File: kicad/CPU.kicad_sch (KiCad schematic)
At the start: 21 parts, among them J1 Conn_ARM_SWD_TagConnect_TC203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, SW1 SW_Push, U5 STM32F303CBTx, X1 8 MHz

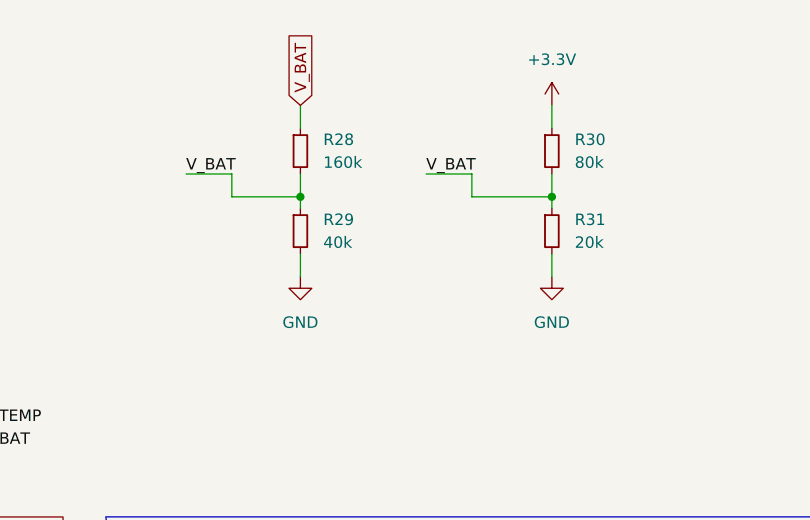
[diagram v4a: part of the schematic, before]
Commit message: [kicad] added thermistor
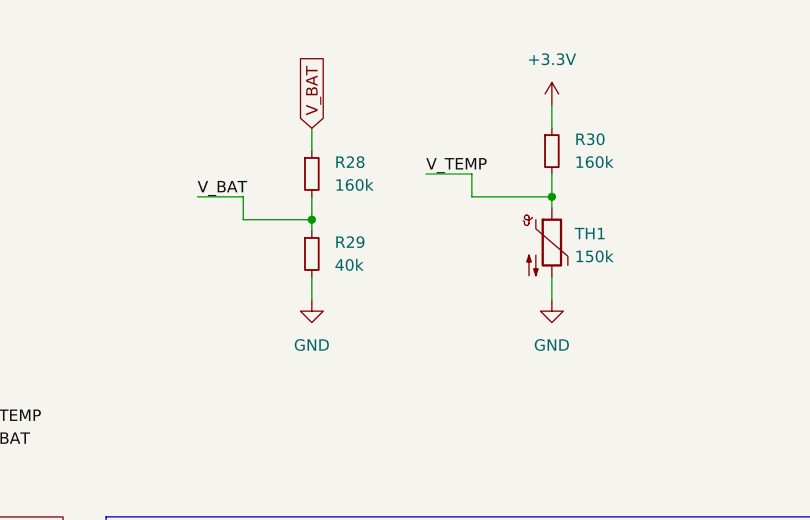
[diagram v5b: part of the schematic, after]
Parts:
- removed R31: 20k, symbol Device:R_Small
- added TH1: 150k, Resistor_SMD:R_0402_1005Metric, symbol Device:Thermistor_NTC
- R30: value 80k -> 160k
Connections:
- net GND: now also TH1.2
- net V_BAT: no longer R30.2
- net V_TEMP: now also R30.2, TH1.1
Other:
- moved on the sheet: R28, R29
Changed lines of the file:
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@@
   (junction (at 85.09 63.5) (diameter 0) (color 0 0 0 0)
   )
-  (junction (at 199.39 34.29) (diameter 0) (color 0 0 0 0)
+  (junction (at 200.66 36.83) (diameter 0) (color 0 0 0 0)
   )
   (junction (at 207.01 82.55) (diameter 0) (color 0 0 0 0)
@@
     (stroke (width 0) (type default))
   )
-  (wire (pts (xy 186.69 31.75) (xy 191.77 31.75))
+  (wire (pts (xy 187.96 34.29) (xy 193.04 34.29))
     (stroke (width 0) (type default))
   )
@@
     (stroke (width 0) (type default))
   )
-  (wire (pts (xy 199.39 34.29) (xy 199.39 35.56))
+  (wire (pts (xy 200.66 36.83) (xy 200.66 38.1))
     (stroke (width 0) (type default))
   )
@@
     (stroke (width 0) (type default))
   )
-  (wire (pts (xy 227.33 40.64) (xy 227.33 43.18))
+  (wire (pts (xy 227.33 43.18) (xy 227.33 45.72))
     (stroke (width 0) (type default))
   )
@@
     (stroke (width 0) (type default))
   )
-  (wire (pts (xy 191.77 34.29) (xy 191.77 31.75))
+  (wire (pts (xy 193.04 36.83) (xy 193.04 34.29))
     (stroke (width 0) (type default))
   )
@@
     (stroke (width 0) (type default))
   )
-  (wire (pts (xy 199.39 40.64) (xy 199.39 43.18))
+  (wire (pts (xy 200.66 43.18) (xy 200.66 45.72))
     (stroke (width 0) (type default))
   )
@@
     (stroke (width 0) (type default))
   )
-  (wire (pts (xy 199.39 34.29) (xy 191.77 34.29))
+  (wire (pts (xy 200.66 36.83) (xy 193.04 36.83))
     (stroke (width 0) (type default))
   )
@@
     (stroke (width 0) (type default))
   )
-  (wire (pts (xy 199.39 24.13) (xy 199.39 26.67))
+  (wire (pts (xy 200.66 26.67) (xy 200.66 29.21))
     (stroke (width 0) (type default))
   )
@@
     (stroke (width 0) (type default))
   )
-  (wire (pts (xy 199.39 31.75) (xy 199.39 34.29))
+  (wire (pts (xy 200.66 34.29) (xy 200.66 36.83))
     (stroke (width 0) (type default))
   )
@@
     (effects (font (size 1.27 1.27)) (justify left bottom))
   )
-  (label "V_BAT" (at 213.36 31.75 0) (fields_autoplaced)
+  (label "V_TEMP" (at 213.36 31.75 0) (fields_autoplaced)
     (effects (font (size 1.27 1.27)) (justify left bottom))
   )
-  (label "V_BAT" (at 186.69 31.75 0) (fields_autoplaced)
+  (label "V_BAT" (at 187.96 34.29 0) (fields_autoplaced)
     (effects (font (size 1.27 1.27)) (justify left bottom))
   )
@@
     )
   )
-  (global_label "V_BAT" (shape input) (at 199.39 24.13 90) (fields_autoplaced)
+  (global_label "V_BAT" (shape input) (at 200.66 26.67 90) (fields_autoplaced)
     (effects (font (size 1.27 1.27)) (justify left))
-    (property "Intersheetrefs" "${INTERSHEET_REFS}" (at 199.39 15.7624 90)
+    (property "Intersheetrefs" "${INTERSHEET_REFS}" (at 200.66 18.3024 90)
       (effects (font (size 1.27 1.27)) (justify left) hide)
     )
@@
     )
   )
-  (symbol (lib_id "power:GND") (at 199.39 43.18 0) (unit 1)
-    (in_bom yes) (on_board yes) (dnp no) (fields_autoplaced)
-    (property "Reference" "#PWR014" (at 199.39 49.53 0)
-      (effects (font (size 1.27 1.27)) hide)
-    )
-    (property "Value" "GND" (at 199.39 48.26 0)
-      (effects (font (size 1.27 1.27)))
-    )
-    (property "Footprint" "" (at 199.39 43.18 0)
-      (effects (font (size 1.27 1.27)) hide)
-    )
-    (property "Datasheet" "" (at 199.39 43.18 0)
+  (symbol (lib_id "power:GND") (at 200.66 45.72 0) (unit 1)
+    (in_bom yes) (on_board yes) (dnp no) (fields_autoplaced)
+    (property "Reference" "#PWR014" (at 200.66 52.07 0)
+      (effects (font (size 1.27 1.27)) hide)
+    )
+    (property "Value" "GND" (at 200.66 50.8 0)
+      (effects (font (size 1.27 1.27)))
+    )
+    (property "Footprint" "" (at 200.66 45.72 0)
+      (effects (font (size 1.27 1.27)) hide)
+    )
+    (property "Datasheet" "" (at 200.66 45.72 0)
       (effects (font (size 1.27 1.27)) hide)
     )
@@
     )
   )
-  (symbol (lib_id "power:GND") (at 227.33 43.18 0) (unit 1)
-    (in_bom yes) (on_board yes) (dnp no) (fields_autoplaced)
-    (property "Reference" "#PWR015" (at 227.33 49.53 0)
-      (effects (font (size 1.27 1.27)) hide)
-    )
-    (property "Value" "GND" (at 227.33 48.26 0)
-      (effects (font (size 1.27 1.27)))
-    )
-    (property "Footprint" "" (at 227.33 43.18 0)
-      (effects (font (size 1.27 1.27)) hide)
-    )
-    (property "Datasheet" "" (at 227.33 43.18 0)
+  (symbol (lib_id "power:GND") (at 227.33 45.72 0) (unit 1)
+    (in_bom yes) (on_board yes) (dnp no) (fields_autoplaced)
+    (property "Reference" "#PWR015" (at 227.33 52.07 0)
+      (effects (font (size 1.27 1.27)) hide)
+    )
+    (property "Value" "GND" (at 227.33 50.8 0)
+      (effects (font (size 1.27 1.27)))
+    )
+    (property "Footprint" "" (at 227.33 45.72 0)
+      (effects (font (size 1.27 1.27)) hide)
+    )
+    (property "Datasheet" "" (at 227.33 45.72 0)
       (effects (font (size 1.27 1.27)) hide)
     )
@@
         (path "/91e2f46a-700b-4d7a-a06a-22469f63223f/7eb1e86b-8a48-408f-b231-0c52f4ea1971"
           (reference "R17") (unit 1)
+        )
+      )
+    )
+  )
+  (symbol (lib_id "Device:Thermistor_NTC") (at 227.33 39.37 0) (unit 1)
+    (in_bom yes) (on_board yes) (dnp no) (fields_autoplaced)
+    (property "Reference" "TH1" (at 229.87 38.4175 0)
+      (effects (font (size 1.27 1.27)) (justify left))
+    )
+    (property "Value" "150k" (at 229.87 40.9575 0)
+      (effects (font (size 1.27 1.27)) (justify left))
+    )
+    (property "Footprint" "Resistor_SMD:R_0402_1005Metric" (at 227.33 38.1 0)
+      (effects (font (size 1.27 1.27)) hide)
+    )
+    (property "Datasheet" "https://www.farnell.com/datasheets/2872294.pdf" (at 227.33 38.1 0)
+      (effects (font (size 1.27 1.27)) hide)
+    )
+    (property "Name" "MURATA NCP15WM154J03RC" (at 227.33 39.37 0)
+      (effects (font (size 1.27 1.27)) hide)
+    )
+    (pin "1")
+    (pin "2")
+    (instances
+      (project "bldc_project"
+        (path "/91e2f46a-700b-4d7a-a06a-22469f63223f/7eb1e86b-8a48-408f-b231-0c52f4ea1971"
+          (reference "TH1") (unit 1)
         )
       )
@@
     )
   )
-  (symbol (lib_id "Device:R_Small") (at 199.39 38.1 0) (unit 1)
-    (in_bom yes) (on_board yes) (dnp no) (fields_autoplaced)
-    (property "Reference" "R29" (at 201.93 36.83 0)
-      (effects (font (size 1.27 1.27)) (justify left))
-    )
-    (property "Value" "40k" (at 201.93 39.37 0)
-      (effects (font (size 1.27 1.27)) (justify left))
-    )
-    (property "Footprint" "" (at 199.39 38.1 0)
-      (effects (font (size 1.27 1.27)) hide)
-    )
-    (property "Datasheet" "~" (at 199.39 38.1 0)
+  (symbol (lib_id "Device:R_Small") (at 200.66 40.64 0) (unit 1)
+    (in_bom yes) (on_board yes) (dnp no) (fields_autoplaced)
+    (property "Reference" "R29" (at 203.2 39.37 0)
+      (effects (font (size 1.27 1.27)) (justify left))
+    )
+    (property "Value" "40k" (at 203.2 41.91 0)
+      (effects (font (size 1.27 1.27)) (justify left))
+    )
+    (property "Footprint" "" (at 200.66 40.64 0)
+      (effects (font (size 1.27 1.27)) hide)
+    )
+    (property "Datasheet" "~" (at 200.66 40.64 0)
       (effects (font (size 1.27 1.27)) hide)
     )
@@
         (path "/91e2f46a-700b-4d7a-a06a-22469f63223f/7eb1e86b-8a48-408f-b231-0c52f4ea1971"
           (reference "R29") (unit 1)
-        )
-      )
-    )
-  )
-  (symbol (lib_id "Device:R_Small") (at 227.33 38.1 0) (unit 1)
-    (in_bom yes) (on_board yes) (dnp no) (fields_autoplaced)
-    (property "Reference" "R31" (at 229.87 36.83 0)
-      (effects (font (size 1.27 1.27)) (justify left))
-    )
-    (property "Value" "20k" (at 229.87 39.37 0)
-      (effects (font (size 1.27 1.27)) (justify left))
-    )
-    (property "Footprint" "" (at 227.33 38.1 0)
-      (effects (font (size 1.27 1.27)) hide)
-    )
-    (property "Datasheet" "~" (at 227.33 38.1 0)
-      (effects (font (size 1.27 1.27)) hide)
-    )
-    (pin "2")
-    (pin "1")
-    (instances
-      (project "bldc_project"
-        (path "/91e2f46a-700b-4d7a-a06a-22469f63223f/7eb1e86b-8a48-408f-b231-0c52f4ea1971"
-          (reference "R31") (unit 1)
         )
       )
@@
     )
   )
-  (symbol (lib_id "Device:R_Small") (at 199.39 29.21 0) (unit 1)
-    (in_bom yes) (on_board yes) (dnp no) (fields_autoplaced)
-    (property "Reference" "R28" (at 201.93 27.94 0)
-      (effects (font (size 1.27 1.27)) (justify left))
-    )
-    (property "Value" "160k" (at 201.93 30.48 0)
-      (effects (font (size 1.27 1.27)) (justify left))
-    )
-    (property "Footprint" "" (at 199.39 29.21 0)
-      (effects (font (size 1.27 1.27)) hide)
-    )
-    (property "Datasheet" "~" (at 199.39 29.21 0)
+  (symbol (lib_id "Device:R_Small") (at 200.66 31.75 0) (unit 1)
+    (in_bom yes) (on_board yes) (dnp no) (fields_autoplaced)
+    (property "Reference" "R28" (at 203.2 30.48 0)
+      (effects (font (size 1.27 1.27)) (justify left))
+    )
+    (property "Value" "160k" (at 203.2 33.02 0)
+      (effects (font (size 1.27 1.27)) (justify left))
+    )
+    (property "Footprint" "" (at 200.66 31.75 0)
+      (effects (font (size 1.27 1.27)) hide)
+    )
+    (property "Datasheet" "~" (at 200.66 31.75 0)
       (effects (font (size 1.27 1.27)) hide)
     )
@@
       (effects (font (size 1.27 1.27)) (justify left))
     )
-    (property "Value" "80k" (at 229.87 30.48 0)
-      (effects (font (size 1.27 1.27)) (justify left))
-    )
+    (property "Value" "160k" (at 229.87 30.48 0)
+      (effects (font (size 1.27 1.27)) (justify left))
+    )

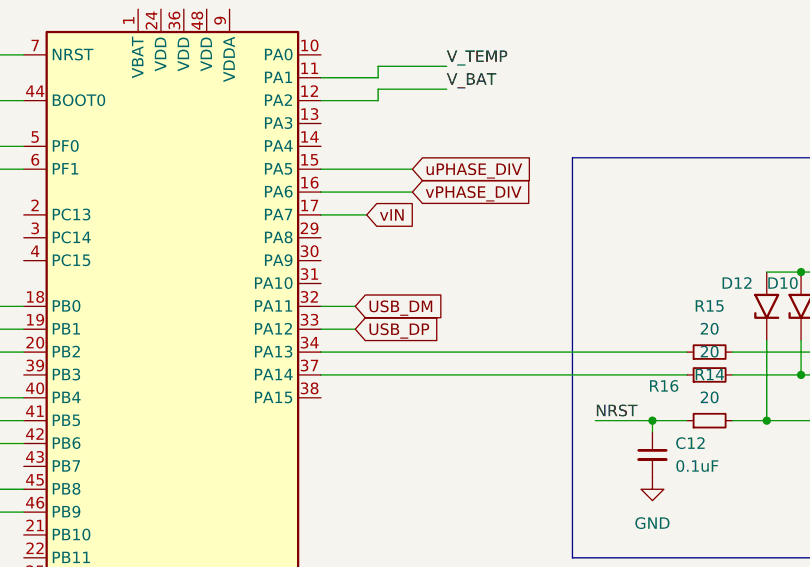
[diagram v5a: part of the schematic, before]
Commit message: Changed USB configuration
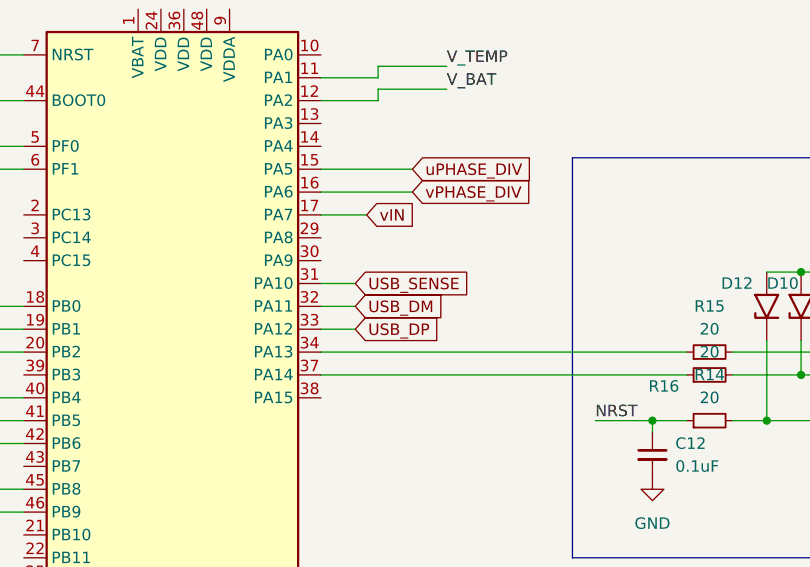
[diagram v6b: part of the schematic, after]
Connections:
- net USB_SENSE: now reaches U5.31 (PA10)
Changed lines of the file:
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@@
+    (stroke (width 0) (type default))
+  )
+  (wire (pts (xy 149.86 83.82) (xy 153.67 83.82))
     (stroke (width 0) (type default))
   )
@@
     )
   )
+  (global_label "USB_SENSE" (shape input) (at 153.67 83.82 0) (fields_autoplaced)
+    (effects (font (size 1.27 1.27)) (justify left))
+    (property "Intersheetrefs" "${INTERSHEET_REFS}" (at 167.4803 83.82 0)
+      (effects (font (size 1.27 1.27)) (justify left) hide)
+    )
+  )

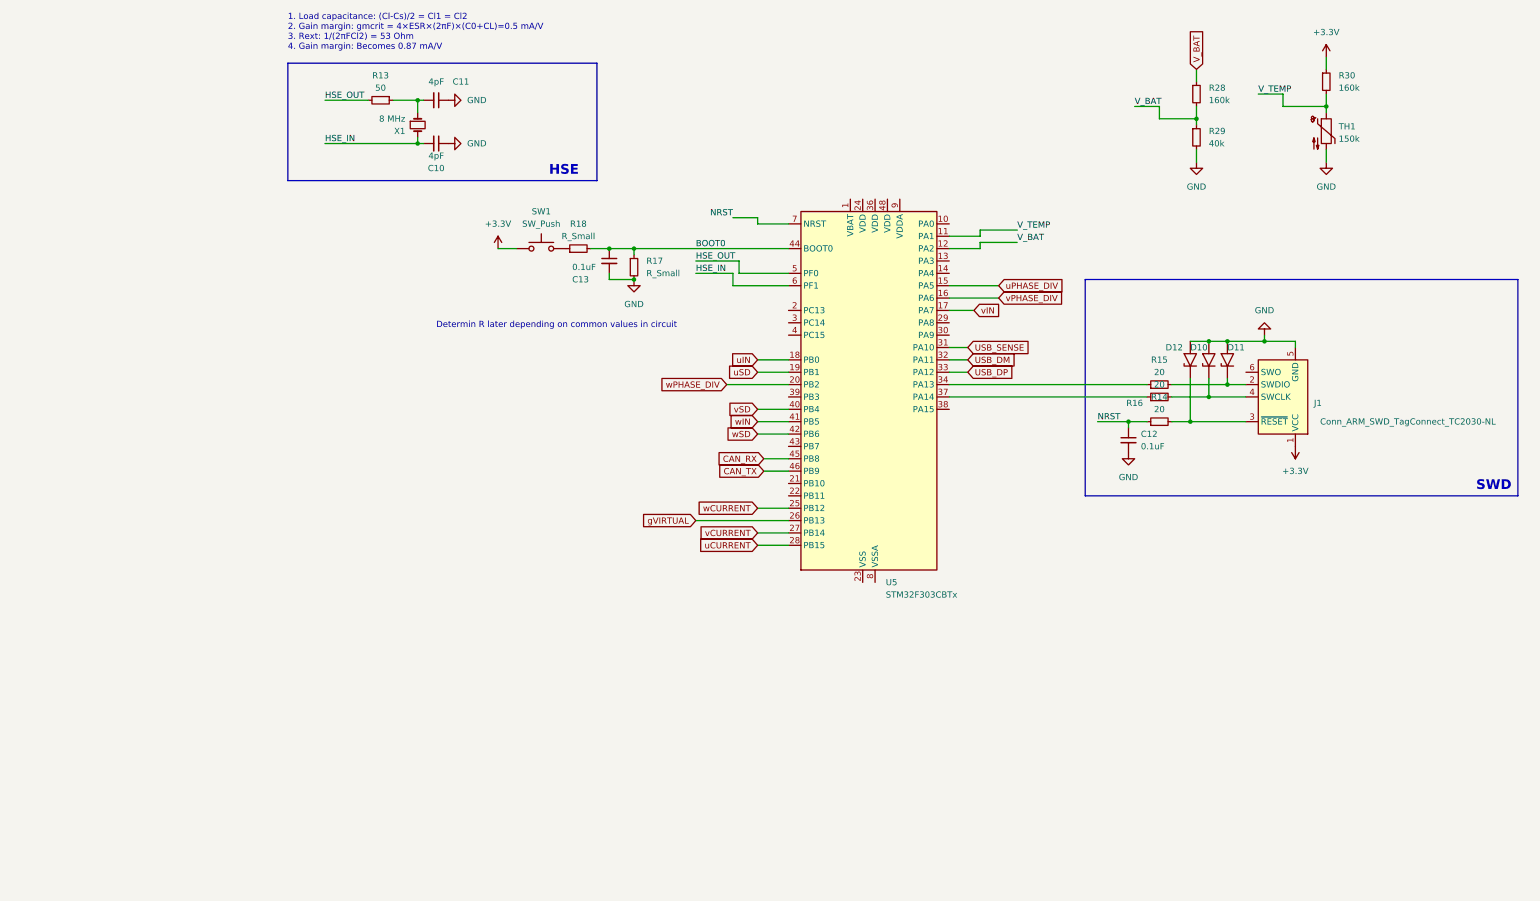
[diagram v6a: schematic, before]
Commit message: [kicad] Added i2c connection
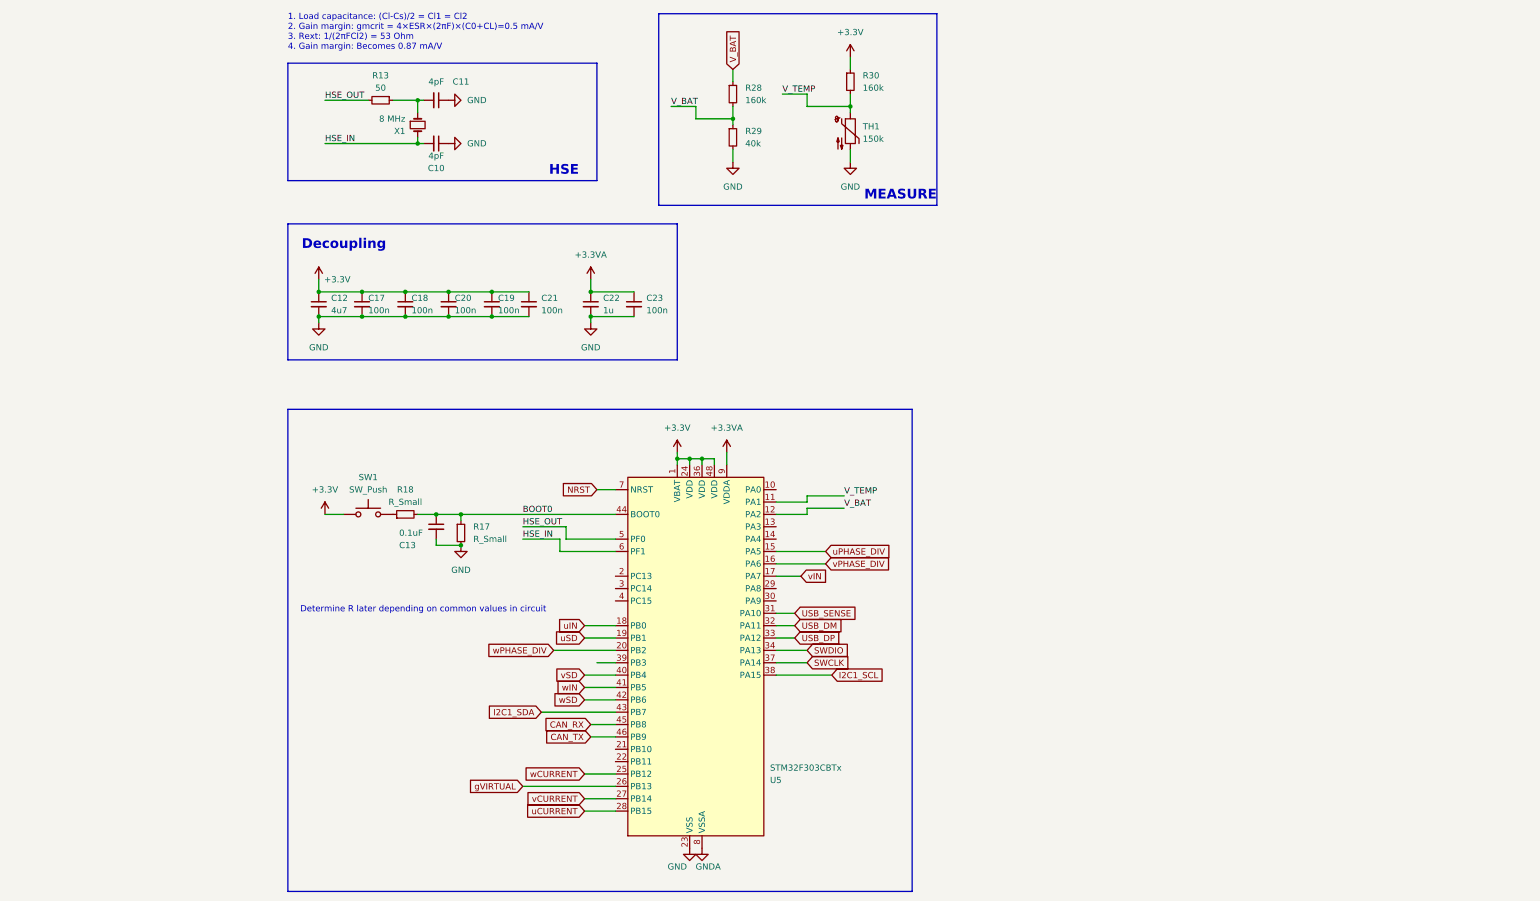
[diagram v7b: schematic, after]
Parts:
- removed D10, D11, D12: SMAJ13A, Diode_SMD:D_SMA, symbol Diode:SMAJ13A
- removed J1: Conn_ARM_SWD_TagConnect_TC2030-NL, Connector:Tag-Connect_TC2030-IDC-NL_2x03_P1.27mm_Vertical, symbol Connector:Conn_ARM_SWD_TagConnect_TC2030-NL
- removed R14, R15, R16: 20, symbol Device:R_Small
- added C17, C18, C19, C20, C21, C23: 100n, symbol Device:C_Small
- added C22: 1u, symbol Device:C_Small
- C12: value 0.1uF -> 4u7
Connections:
- net +3.3V: now also C12.1, U5.1 (VBAT), U5.24 (VDD), U5.36 (VDD), U5.48 (VDD), C17.1, C18.1, C19.1, C20.1, C21.1
- net GND: now also U5.23 (VSS), U5.35 (VSS), U5.47 (VSS), C17.2, C18.2, C19.2, C20.2, C21.2, C22.2, C23.2
- net NRST: no longer C12.1
- net SWDIO: now reaches U5.34 (PA13)
- net SWCLK: now reaches U5.37 (PA14)
- net I2C1_SCL: now reaches U5.38 (PA15)
- net I2C1_SDA: now reaches U5.43 (PB7)
- net GNDA: now reaches U5.8 (VSSA)
- net +3.3VA: now reaches U5.9 (VDDA)
- net +3.3VA: now also C22.1, C23.1
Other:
- note added: "Determine R later depending on common values in circuit"
- note removed: "Determin R later depending on common values in circuit"
- moved on the sheet: C13, R17, R18, R28, R29, R30, SW1, TH1, U5
